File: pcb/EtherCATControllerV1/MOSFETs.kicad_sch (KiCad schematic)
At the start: 21 parts

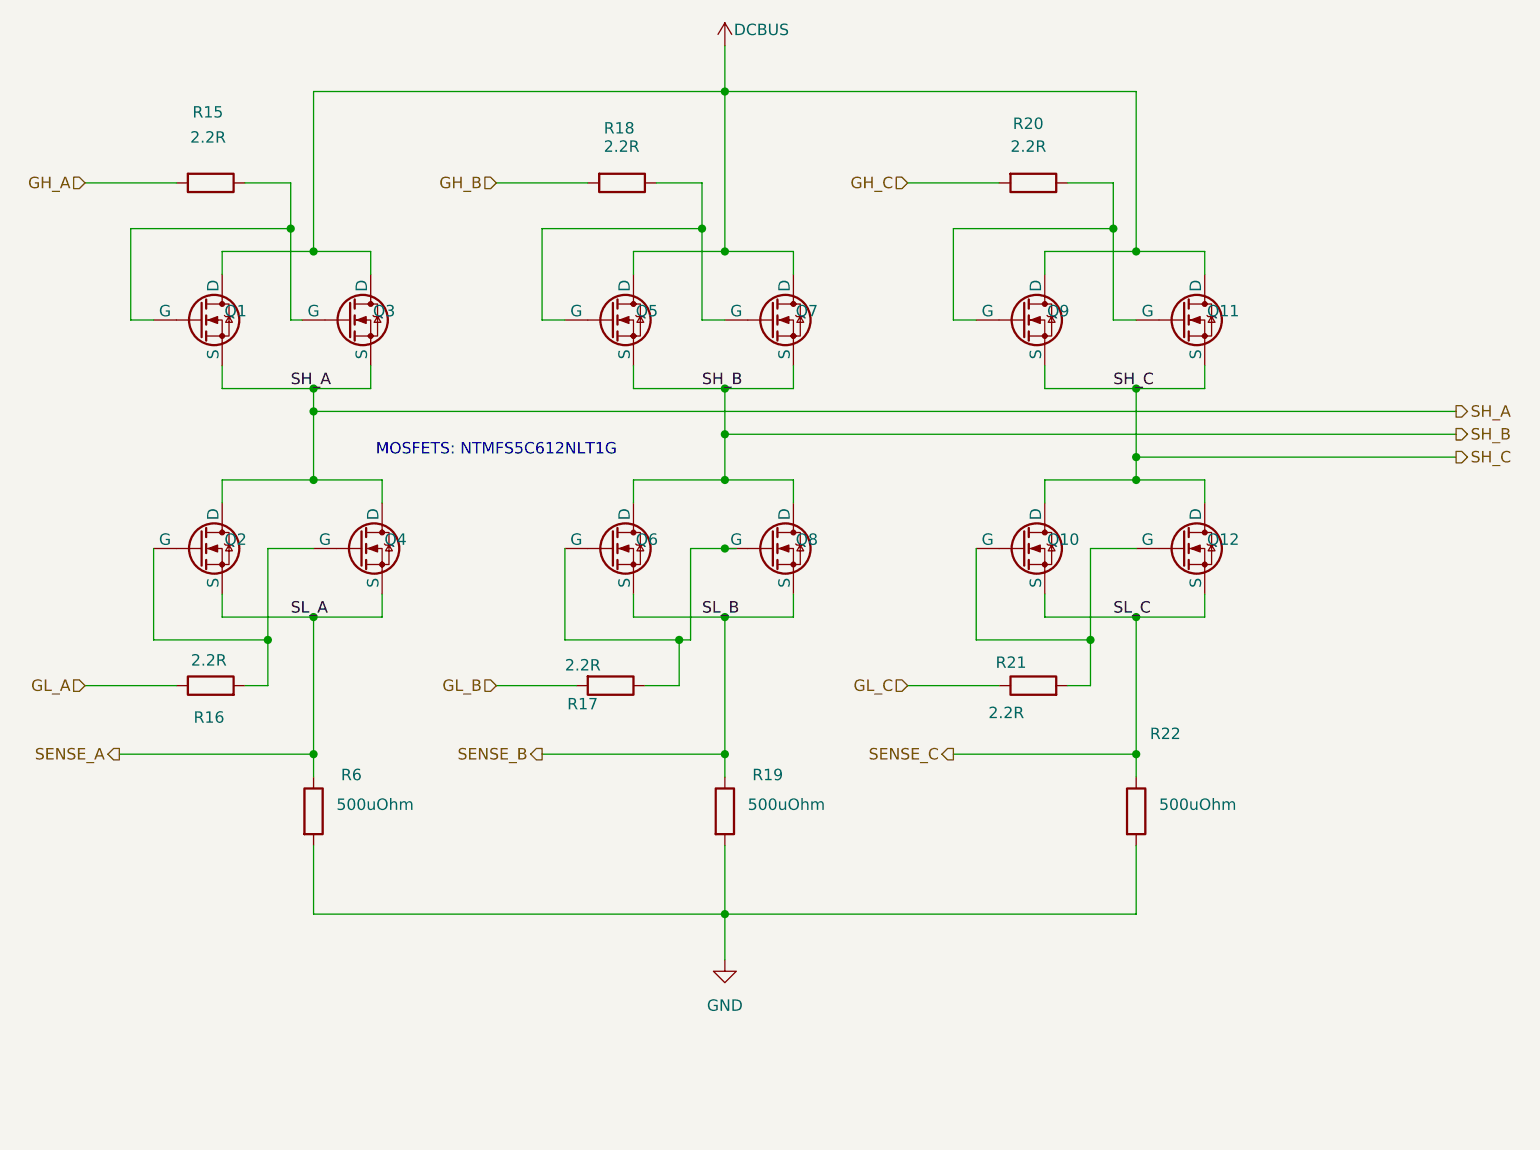
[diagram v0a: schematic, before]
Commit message: Initial design without Ethernet connectors
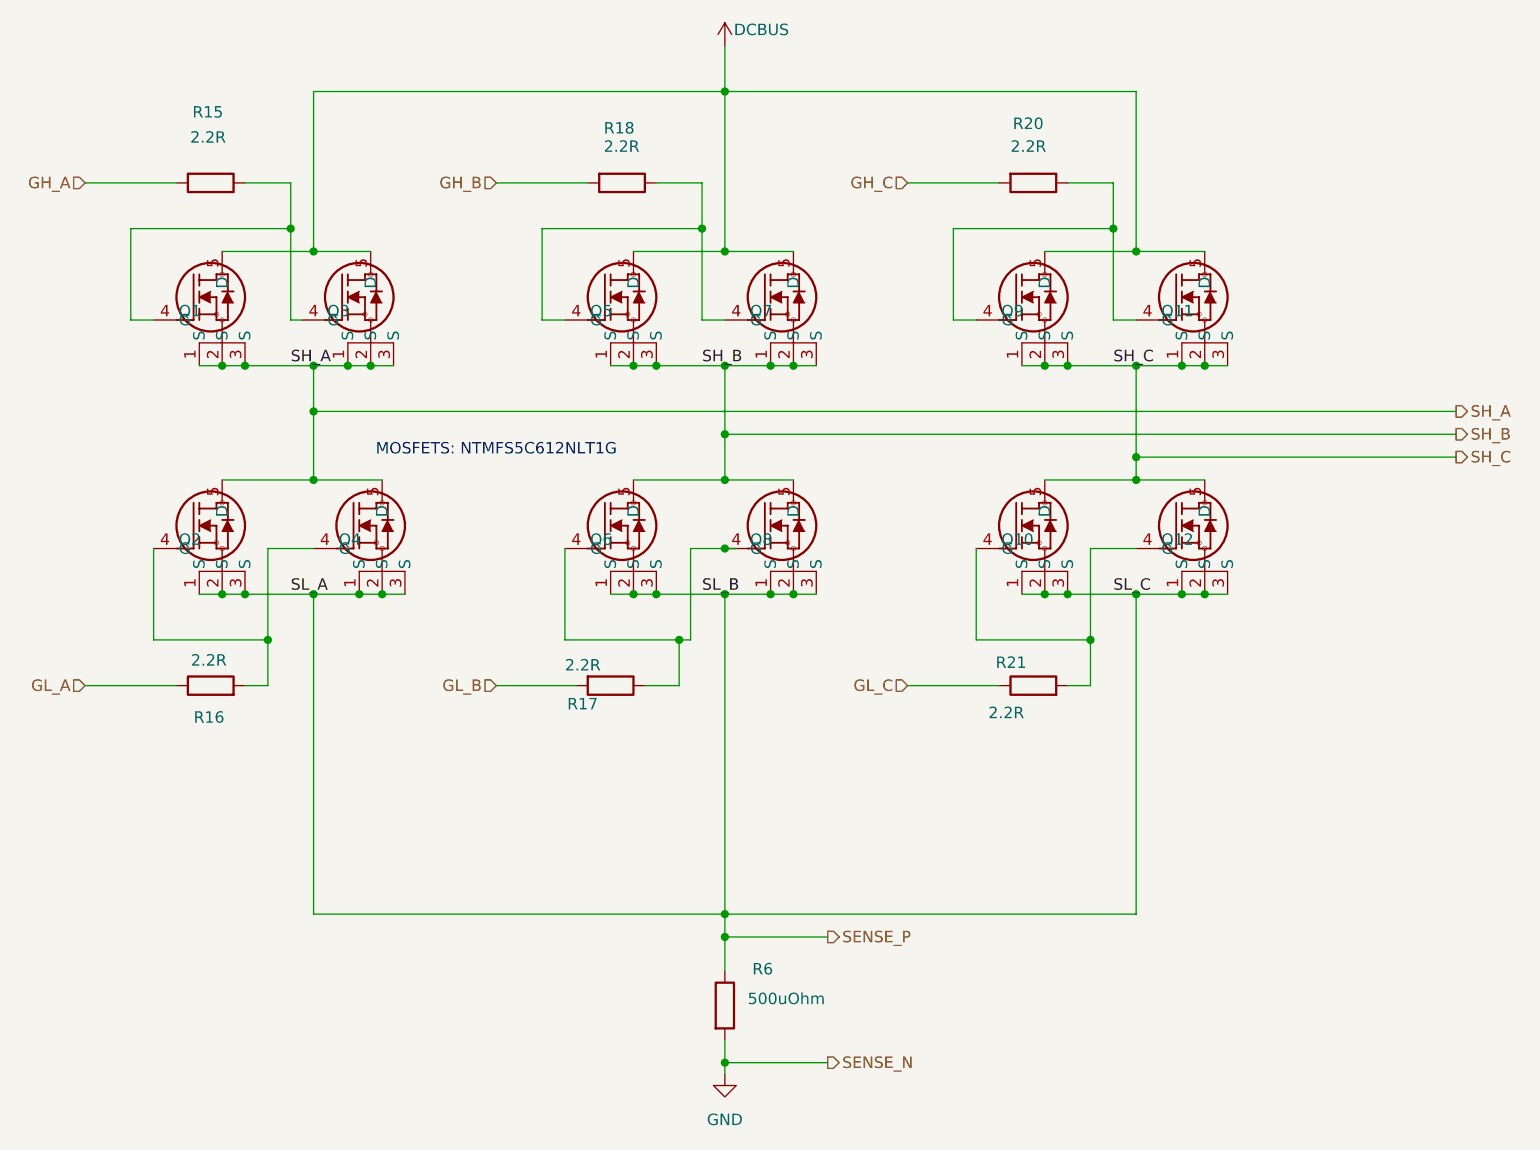
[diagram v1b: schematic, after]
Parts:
- removed R19, R22: 500uOhm, Resistor_SMD:R_2512_6332Metric, symbol Device:R
- Q1, Q10, Q11, Q12, Q2, Q3, Q4, Q5, Q6, Q7, Q8, Q9: footprint Package_SO:ONSemi_SO-8FL_488AA -> DFN_2NLT1G_ONS; symbol CustomNMOS:NMOS_1 -> 2024-07-02_05-47-45:NTMFS5C612NLT1G
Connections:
- net SENSE_B is gone; now on net SENSE_P: Q6.1 (S), Q8.1 (S)
- net SENSE_C is gone; now on net SENSE_P: Q10.1 (S), Q12.1 (S)
- net SH_A: now also Q1.2 (S), Q1.3 (S), Q3.2 (S), Q3.3 (S)
- net SH_B: now also Q5.2 (S), Q5.3 (S), Q7.2 (S), Q7.3 (S)
- net SH_C: now also Q11.2 (S), Q11.3 (S), Q9.2 (S), Q9.3 (S)
- net SENSE_A renamed SENSE_P
- net SENSE_P: now also Q10.2 (S), Q10.3 (S), Q12.2 (S), Q12.3 (S), Q2.2 (S), Q2.3 (S), Q4.2 (S), Q4.3 (S), Q6.2 (S), Q6.3 (S), Q8.2 (S), Q8.3 (S)

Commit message: Added IO Board project
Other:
- note added: "MOSFETS: NTMFS5C612NLT1G 60V, 36A Ta"
- note removed: "MOSFETS: NTMFS5C612NLT1G"
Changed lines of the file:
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@@
 		)
 	)
-	(text "MOSFETS: NTMFS5C612NLT1G"
+	(text "MOSFETS: NTMFS5C612NLT1G\n60V, 36A Ta"
 		(exclude_from_sim no)
 		(at 105.41 86.36 0)

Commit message: fix all ERCs
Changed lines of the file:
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@@
 	)
 	(junction
+		(at 162.56 137.16)
+		(diameter 0)
+		(color 0 0 0 0)
+	)
+	(junction
 		(at 184.15 101.6)
 		(diameter 0)
@@
 	(wire
 		(pts
-			(xy 130.81 137.16) (xy 176.53 137.16)
+			(xy 130.81 137.16) (xy 162.56 137.16)
 		)
 		(stroke
@@
 	(wire
 		(pts
+			(xy 162.56 137.16) (xy 176.53 137.16)
+		)
+		(stroke
+			(width 0)
+			(type default)
+		)
+	)
+	(wire
+		(pts
 			(xy 166.37 88.9) (xy 176.53 88.9)
 		)
@@
 	)
 	(symbol
+		(lib_name "NTMFS5C612NLT1G_3")
 		(lib_id "2024-07-02_05-47-45:NTMFS5C612NLT1G")
 		(at 67.31 71.12 0)
@@
 			)
 		)
+		(property "LCSC Part Number" ""
+			(at 67.31 71.12 0)
+			(effects
+				(font
+					(size 1.27 1.27)
+				)
+				(hide yes)
+			)
+		)
 		(pin "1"
 		)
@@
 	)
 	(symbol
+		(lib_name "NTMFS5C612NLT1G_5")
 		(lib_id "2024-07-02_05-47-45:NTMFS5C612NLT1G")
 		(at 176.53 71.12 0)
@@
 	)
 	(symbol
+		(lib_name "NTMFS5C612NLT1G_2")
 		(lib_id "2024-07-02_05-47-45:NTMFS5C612NLT1G")
 		(at 113.03 71.12 0)
@@
 	)
 	(symbol
+		(lib_id "power:PWR_FLAG")
+		(at 162.56 137.16 180)
+		(unit 1)
+		(exclude_from_sim no)
+		(in_bom yes)
+		(on_board yes)
+		(dnp no)
+		(fields_autoplaced yes)
+		(property "Reference" "#FLG011"
+			(at 162.56 139.065 0)
+			(effects
+				(font
+					(size 1.27 1.27)
+				)
+				(hide yes)
+			)
+		)
+		(property "Value" "PWR_FLAG"
+			(at 162.56 142.24 0)
+			(effects
+				(font
+					(size 1.27 1.27)
+				)
+			)
+		)
+		(property "Footprint" ""
+			(at 162.56 137.16 0)
+			(effects
+				(font
+					(size 1.27 1.27)
+				)
+				(hide yes)
+			)
+		)
+		(property "Datasheet" "~"
+			(at 162.56 137.16 0)
+			(effects
+				(font
+					(size 1.27 1.27)
+				)
+				(hide yes)
+			)
+		)
+		(property "Description" "Special symbol for telling ERC where power comes from"
+			(at 162.56 137.16 0)
+			(effects
+				(font
+					(size 1.27 1.27)
+				)
+				(hide yes)
+			)
+		)
+		(pin "1"
+		)
+		(instances
+			(project ""
+				(path "/4c927f80-855d-490a-80b2-e5c55283621a/b8886fcf-711b-4283-9745-a57e39aa3085/55580437-8668-4251-b652-b45caec55db3"
+					(reference "#FLG011")
+					(unit 1)
+				)
+			)
+		)
+	)
+	(symbol
+		(lib_name "NTMFS5C612NLT1G_4")
 		(lib_id "2024-07-02_05-47-45:NTMFS5C612NLT1G")
 		(at 158.75 71.12 0)
@@
 	)
 	(symbol
+		(lib_name "NTMFS5C612NLT1G_1")
 		(lib_id "2024-07-02_05-47-45:NTMFS5C612NLT1G")
 		(at 83.82 71.12 0)
@@
 	)
 	(symbol
+		(lib_name "NTMFS5C612NLT1G_6")
 		(lib_id "2024-07-02_05-47-45:NTMFS5C612NLT1G")
 		(at 130.81 71.12 0)
@@
 			(effects
 				(font
+					(size 1.27 1.27)
+				)
+				(hide yes)
+			)
+		)
+		(property "LCSC Part Number" ""
+			(at 67.31 96.52 0)
+			(effects
+				(font

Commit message: Added more BOM items
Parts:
- Q1, Q3: LCSC Part Number (none) -> C348543
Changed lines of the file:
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@@
 			)
 		)
-		(property "LCSC Part Number" ""
+		(property "LCSC Part Number" "C348543"
 			(at 67.31 71.12 0)
 			(effects
@@
 				(hide yes)
 			)
+		)
+		(property "LCSC Part Number" "C348543"
+			(at 83.82 71.12 0)
+			(effects
+				(font
+					(size 1.27 1.27)
+				)
+				(hide yes)
+			)
